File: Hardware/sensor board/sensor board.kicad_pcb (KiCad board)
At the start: 2 copper layers, 73.9 x 55.9 mm, 11 parts, among them J1 Raspberry_Pi_2_3, J2 Bar30, J3 LPS331AP, J4 Conn_01x04_Pin, J5 Conn_01x04_Pin, U1 MTi_3

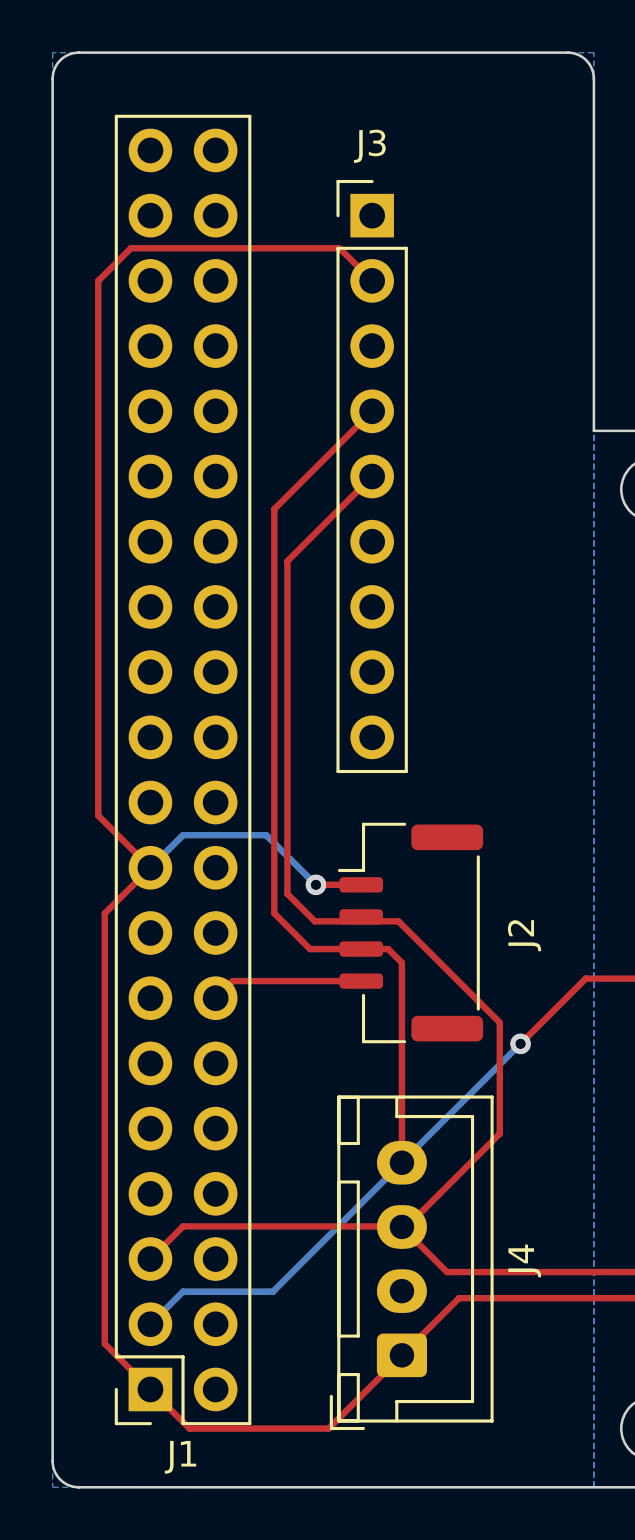
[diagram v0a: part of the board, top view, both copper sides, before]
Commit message: fixed rpi header orientation
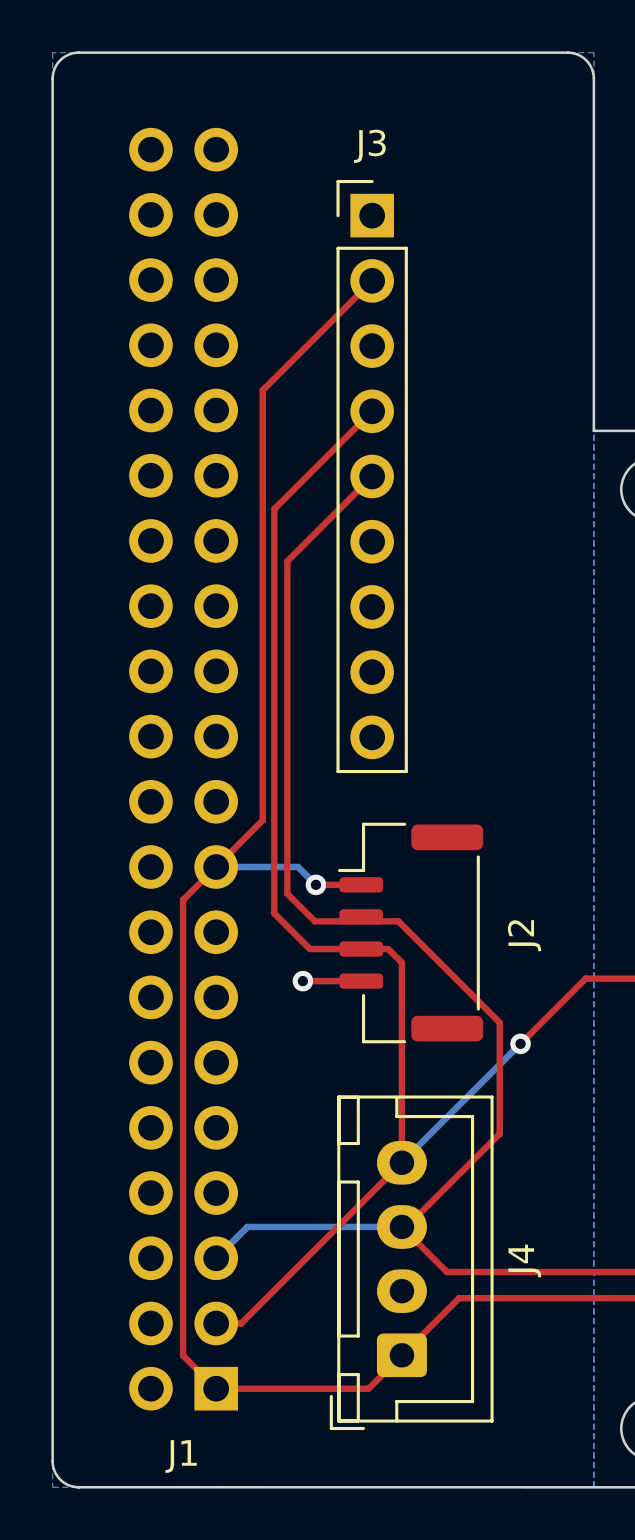
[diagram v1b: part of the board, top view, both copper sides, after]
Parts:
- J1: moved to B.Cu
- moved J1 2.56 mm to (24.7, 67.8), turned to 0 degrees
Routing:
- net +3.3V: track 158.6 -> 140.7 mm
- net GND: track 17.9 -> 14.2 mm, vias 0 -> 1
- net /SDA: track 113.3 -> 110.7 mm
- net /SCL: track 119.3 -> 116.7 mm
